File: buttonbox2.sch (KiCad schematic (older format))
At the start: 58 parts, among them J2 AVR-PDI-6, J4 Conn_01x03_Male, SW1 SW_SP3T, SW10 SW_Push, SW11 SW_Push, SW12 SW_Push, SW13 SW_Push, SW14 SW_Push, SW15 SW_Push, SW16 SW_Push, SW17 SW_Push, SW18 SW_Push, SW19 SW_Push, SW20 SW_Push, SW21 SW_Push, SW22 SW_Push, SW23 SW_Push, SW24 SW_Push, SW25 SW_Push, SW26 SW_Push, SW27 SW_Push, SW28 SW_Push, SW29 SW_Push, SW30 SW_Push, SW31 SW_Push, SW32 SW_Push, SW33 SW_Push, SW34 SW_Push, SW35 SW_Push, SW36 SW_Push, SW37 SW_Push, SW38 SW_Push, SW39 SW_Push, SW40 SW_Push, SW5 SW_Push, SW6 SW_Push, SW7 SW_Push, SW8 SW_Push, SW9 SW_Push, U1 ATxmega256A3-AU, U6 AMS1117-3.3, Y2 Crystal_GND24

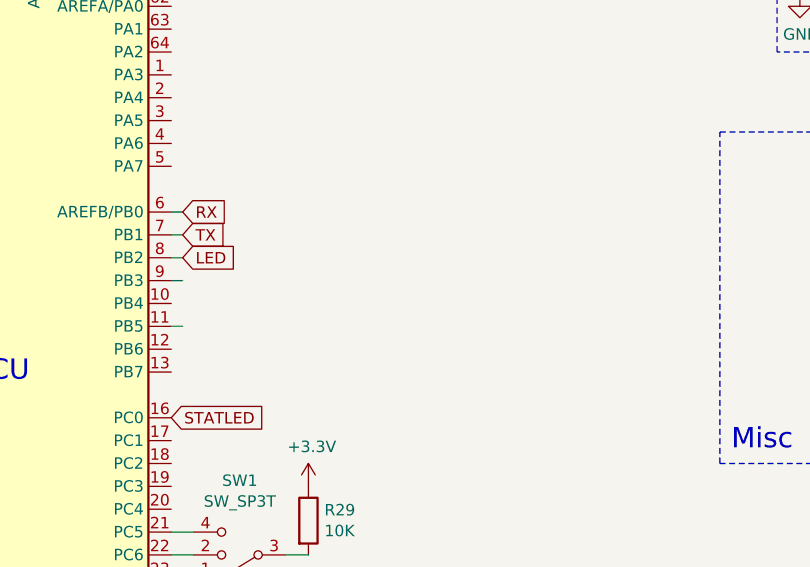
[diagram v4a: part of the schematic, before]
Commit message: Added a rotary encoder and almost all BC values
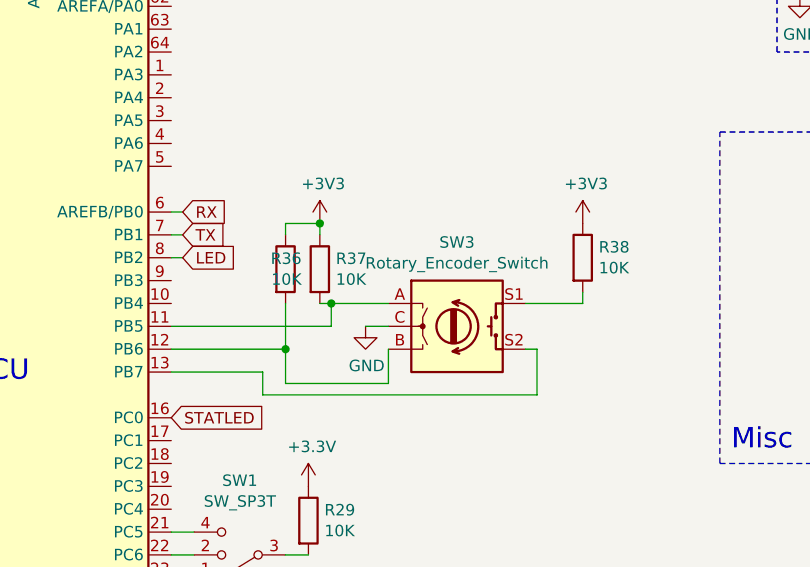
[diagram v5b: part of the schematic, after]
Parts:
- added R36, R37, R38: 10K, Resistor_SMD:R_0805_2012Metric, symbol Device:R
- added SW3: Rotary_Encoder_Switch, Rotary_Encoder:RotaryEncoder_Alps_EC11E-Switch_Vertical_H20mm_CircularMountingHoles, symbol Device:Rotary_Encoder_Switch
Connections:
- net +3V3: now also R36.1, R37.1, R38.1
- net GND: now also SW3.C
- net at U1.11 (PB5): now also R37.2, SW3.A
- net at U1.12 (PB6): now also R36.2, SW3.B
- net at U1.13 (PB7): now also SW3.S2
- new net: R38.2, SW3.S1
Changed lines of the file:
@@
 	2600 1200 2600 1100
 Connection ~ 2600 1200
-Wire Wire Line
-	3350 2750 3300 2750
-Wire Wire Line
-	3300 2950 3350 2950
 $Comp
 L power:GND #PWR04
@@
 	1350 2100 1900 2100
 Connection ~ 750  2100
+$Comp
+L Device:Rotary_Encoder_Switch SW3
+U 1 1 60C1C70F
+P 4550 2950
+F 0 "SW3" H 4550 3317 50  0000 C CNN
+F 1 "Rotary_Encoder_Switch" H 4550 3226 50  0000 C CNN
+F 2 "Rotary_Encoder:RotaryEncoder_Alps_EC11E-Switch_Vertical_H20mm_CircularMountingHoles" H 4400 3110 50  0001 C CNN
+F 3 "~" H 4550 3210 50  0001 C CNN
+	1    4550 2950
+	1    0    0    -1
+$EndComp
+$Comp
+L power:+3V3 #PWR054
+U 1 1 60CA26ED
+P 3950 2500
+F 0 "#PWR054" H 3950 2350 50  0001 C CNN
+F 1 "+3V3" H 3965 2673 50  0000 C CNN
+F 2 "" H 3950 2500 50  0001 C CNN
+F 3 "" H 3950 2500 50  0001 C CNN
+	1    3950 2500
+	1    0    0    -1
+$EndComp
+$Comp
+L power:GND #PWR055
+U 1 1 60CA3341
+P 4150 2950
+F 0 "#PWR055" H 4150 2700 50  0001 C CNN
+F 1 "GND" H 4155 2777 50  0000 C CNN
+F 2 "" H 4150 2950 50  0001 C CNN
+F 3 "" H 4150 2950 50  0001 C CNN
+	1    4150 2950
+	1    0    0    -1
+$EndComp
+Wire Wire Line
+	4250 2950 4150 2950
+$Comp
+L Device:R R37
+U 1 1 60CC5806
+P 3950 2700
+F 0 "R37" H 4020 2746 50  0000 L CNN
+F 1 "10K" H 4020 2655 50  0000 L CNN
+F 2 "Resistor_SMD:R_0805_2012Metric" V 3880 2700 50  0001 C CNN
+F 3 "~" H 3950 2700 50  0001 C CNN
+	1    3950 2700
+	1    0    0    -1
+$EndComp
+Wire Wire Line
+	3950 2850 4000 2850
+$Comp
+L Device:R R36
+U 1 1 60CFB51D
+P 3800 2700
+F 0 "R36" H 3870 2746 50  0000 R CNN
+F 1 "10K" H 3870 2655 50  0000 R CNN
+F 2 "Resistor_SMD:R_0805_2012Metric" V 3730 2700 50  0001 C CNN
+F 3 "~" H 3800 2700 50  0001 C CNN
+	1    3800 2700
+	1    0    0    -1
+$EndComp
+Wire Wire Line
+	3800 2550 3800 2500
+Wire Wire Line
+	3800 2500 3950 2500
+Wire Wire Line
+	3950 2550 3950 2500
+Connection ~ 3950 2500
+Wire Wire Line
+	4250 3050 4250 3200
+Wire Wire Line
+	4250 3200 3800 3200
+Wire Wire Line
+	3800 3200 3800 3050
+Wire Wire Line
+	4000 2850 4000 2950
+Wire Wire Line
+	4000 2950 3300 2950
+Connection ~ 4000 2850
+Wire Wire Line
+	4000 2850 4250 2850
+Wire Wire Line
+	3800 3050 3300 3050
+Connection ~ 3800 3050
+Wire Wire Line
+	3800 3050 3800 2850
+$Comp
+L power:+3V3 #PWR056
+U 1 1 60D421AA
+P 5100 2500
+F 0 "#PWR056" H 5100 2350 50  0001 C CNN
+F 1 "+3V3" H 5115 2673 50  0000 C CNN
+F 2 "" H 5100 2500 50  0001 C CNN
+F 3 "" H 5100 2500 50  0001 C CNN
+	1    5100 2500
+	1    0    0    -1
+$EndComp
+Wire Wire Line
+	4850 2850 5100 2850
+Wire Wire Line
+	5100 2850 5100 2800
+Wire Wire Line
+	4900 3050 4900 3250
+Wire Wire Line
+	3700 3250 3700 3150
+Wire Wire Line
+	3700 3150 3300 3150
+Wire Wire Line
+	4850 3050 4900 3050
+Wire Wire Line
+	3700 3250 4900 3250
+$Comp
+L Device:R R38
+U 1 1 60D8FC06
+P 5100 2650
+F 0 "R38" H 5170 2696 50  0000 L CNN
+F 1 "10K" H 5170 2605 50  0000 L CNN
+F 2 "Resistor_SMD:R_0805_2012Metric" V 5030 2650 50  0001 C CNN
+F 3 "~" H 5100 2650 50  0001 C CNN
+	1    5100 2650
+	1    0    0    -1
+$EndComp
 $EndSCHEMATC

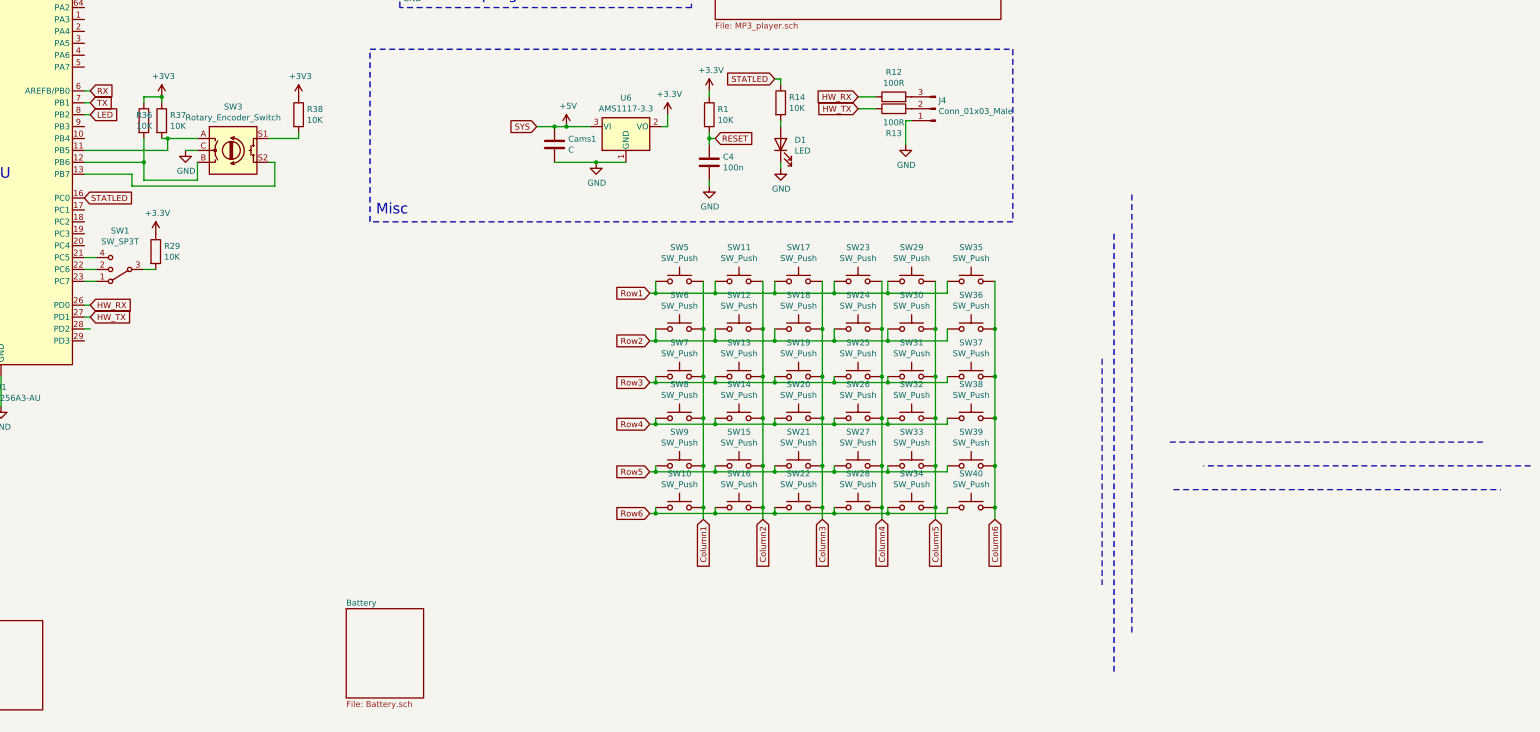
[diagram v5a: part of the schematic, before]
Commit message: Final schematic edits, PCB layout
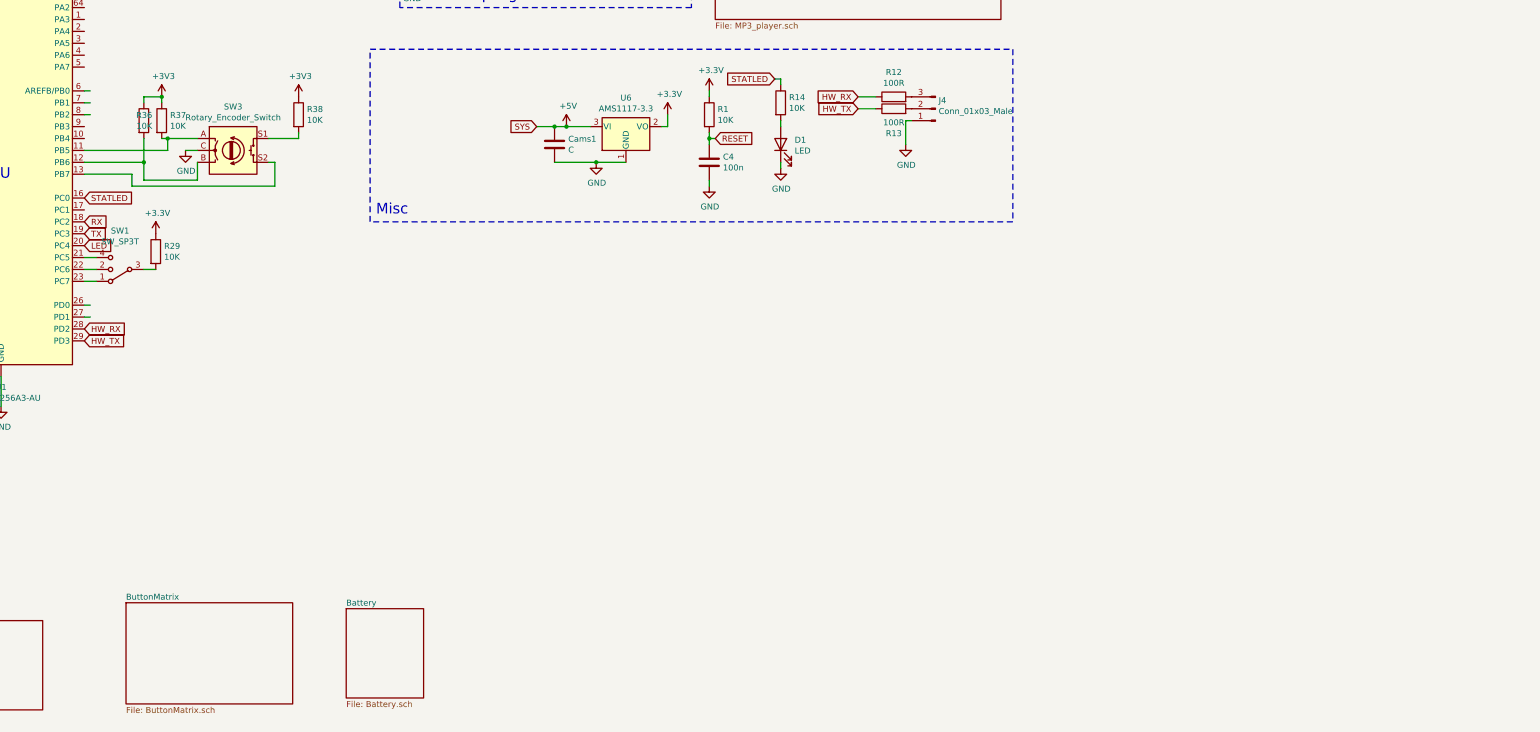
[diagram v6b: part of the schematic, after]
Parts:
- removed SW10, SW11, SW12, SW13, SW14, SW15, SW16, SW17, SW18, SW19, SW20, SW21, SW22, SW23, SW24, SW25, SW26, SW27, SW28, SW29, SW30, SW31, SW32, SW33, SW34, SW35, SW36, SW37, SW38, SW39, SW40, SW5, SW6, SW7, SW8, SW9: SW_Push, Hardware:SW_Cherry_MX_1.00u_PCB_BETTER, symbol Switch:SW_Push
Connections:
- wire segments 209 -> 100

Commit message: pretty much routed everything
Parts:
- added C37, C38, C39: 100n, Capacitor_SMD:C_0805_2012Metric, symbol Device:C
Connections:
- wire segments 100 -> 106
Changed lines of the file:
@@
 	4250 3050 4250 3200
 Wire Wire Line
-	4250 3200 3800 3200
+	4250 3200 4100 3200
 Wire Wire Line
 	3800 3200 3800 3050
@@
 Connection ~ 4000 2850
 Wire Wire Line
-	4000 2850 4250 2850
-Wire Wire Line
-	3800 3050 3300 3050
+	4000 2850 4150 2850
 Connection ~ 3800 3050
 Wire Wire Line
@@
 Wire Wire Line
 	4850 3050 4900 3050
-Wire Wire Line
-	3700 3250 4900 3250
 $Comp
 L Device:R R38
@@
 F1 "ButtonMatrix.sch" 50
 $EndSheet
+$Comp
+L Device:C C38
+U 1 1 610B68E6
+P 4150 2700
+F 0 "C38" H 4265 2746 50  0000 L CNN
+F 1 "100n" H 4265 2655 50  0000 L CNN
+F 2 "Capacitor_SMD:C_0805_2012Metric" H 4188 2550 50  0001 C CNN
+F 3 "~" H 4150 2700 50  0001 C CNN
+	1    4150 2700
+	1    0    0    -1
+$EndComp
+Connection ~ 4150 2850
+Wire Wire Line
+	4150 2850 4250 2850
+$Comp
+L Device:C C37
+U 1 1 610B785E
+P 4100 3350
+F 0 "C37" H 4215 3396 50  0000 L CNN
+F 1 "100n" H 4215 3305 50  0000 L CNN
+F 2 "Capacitor_SMD:C_0805_2012Metric" H 4138 3200 50  0001 C CNN
+F 3 "~" H 4100 3350 50  0001 C CNN
+	1    4100 3350
+	1    0    0    -1
+$EndComp
+Connection ~ 4100 3200
+Wire Wire Line
+	4100 3200 3800 3200
+Wire Wire Line
+	3300 3050 3800 3050
+$Comp
+L power:GND #PWR057
+U 1 1 610BB4E5
+P 4100 3500
+F 0 "#PWR057" H 4100 3250 50  0001 C CNN
+F 1 "GND" H 4105 3327 50  0000 C CNN
+F 2 "" H 4100 3500 50  0001 C CNN
+F 3 "" H 4100 3500 50  0001 C CNN
+	1    4100 3500
+	1    0    0    -1
+$EndComp
+$Comp
+L power:GND #PWR058
+U 1 1 610BBB62
+P 4400 2400
+F 0 "#PWR058" H 4400 2150 50  0001 C CNN
+F 1 "GND" H 4405 2227 50  0000 C CNN
+F 2 "" H 4400 2400 50  0001 C CNN
+F 3 "" H 4400 2400 50  0001 C CNN
+	1    4400 2400
+	1    0    0    -1
+$EndComp
+$Comp
+L power:GND #PWR059
+U 1 1 610BC44A
+P 4850 3550
+F 0 "#PWR059" H 4850 3300 50  0001 C CNN
+F 1 "GND" H 4855 3377 50  0000 C CNN
+F 2 "" H 4850 3550 50  0001 C CNN
+F 3 "" H 4850 3550 50  0001 C CNN
+	1    4850 3550
+	1    0    0    -1
+$EndComp
+Wire Wire Line
+	4150 2300 4150 2550
+Wire Wire Line
+	4150 2300 4400 2300
+Wire Wire Line
+	4400 2300 4400 2400
+Wire Wire Line
+	3700 3250 4850 3250
+$Comp
+L Device:C C39
+U 1 1 610D8766
+P 4850 3400
+F 0 "C39" H 4965 3446 50  0000 L CNN
+F 1 "100n" H 4965 3355 50  0000 L CNN
+F 2 "Capacitor_SMD:C_0805_2012Metric" H 4888 3250 50  0001 C CNN
+F 3 "~" H 4850 3400 50  0001 C CNN
+	1    4850 3400
+	1    0    0    -1
+$EndComp
+Connection ~ 4850 3250
+Wire Wire Line
+	4850 3250 4900 3250
 $EndSCHEMATC

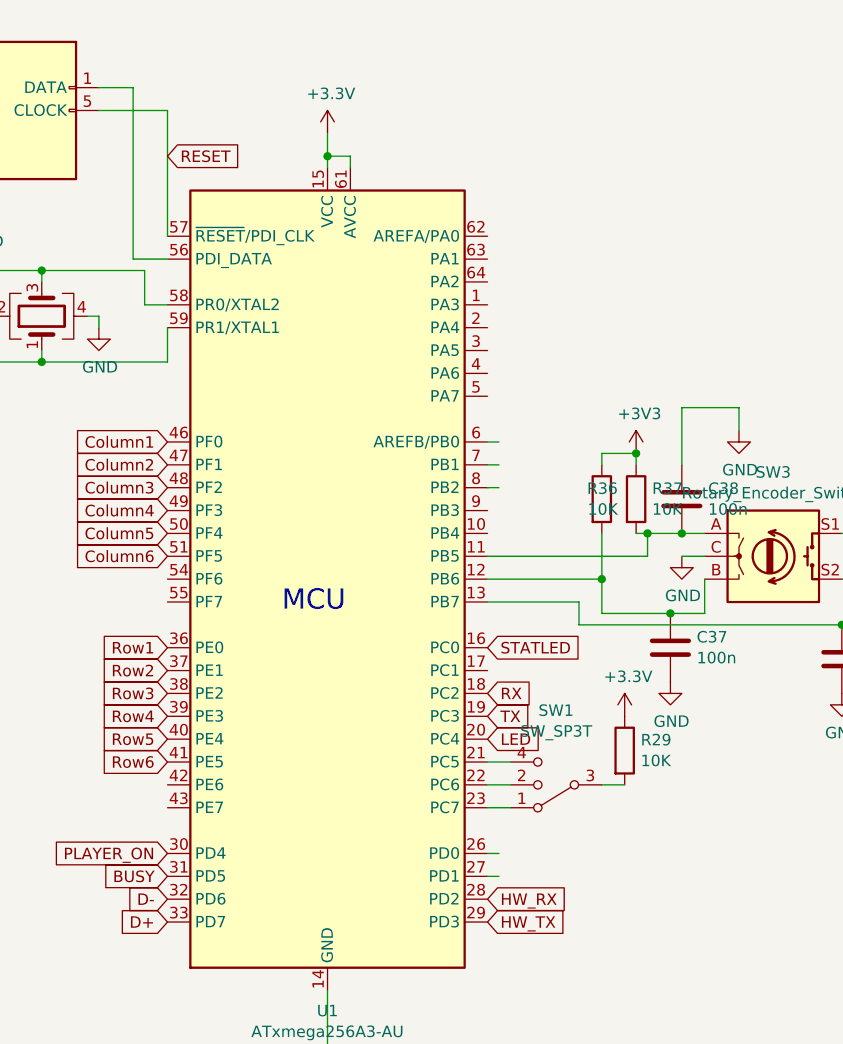
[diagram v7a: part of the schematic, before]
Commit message: Fixed some DRC errors and some incorrect wiring
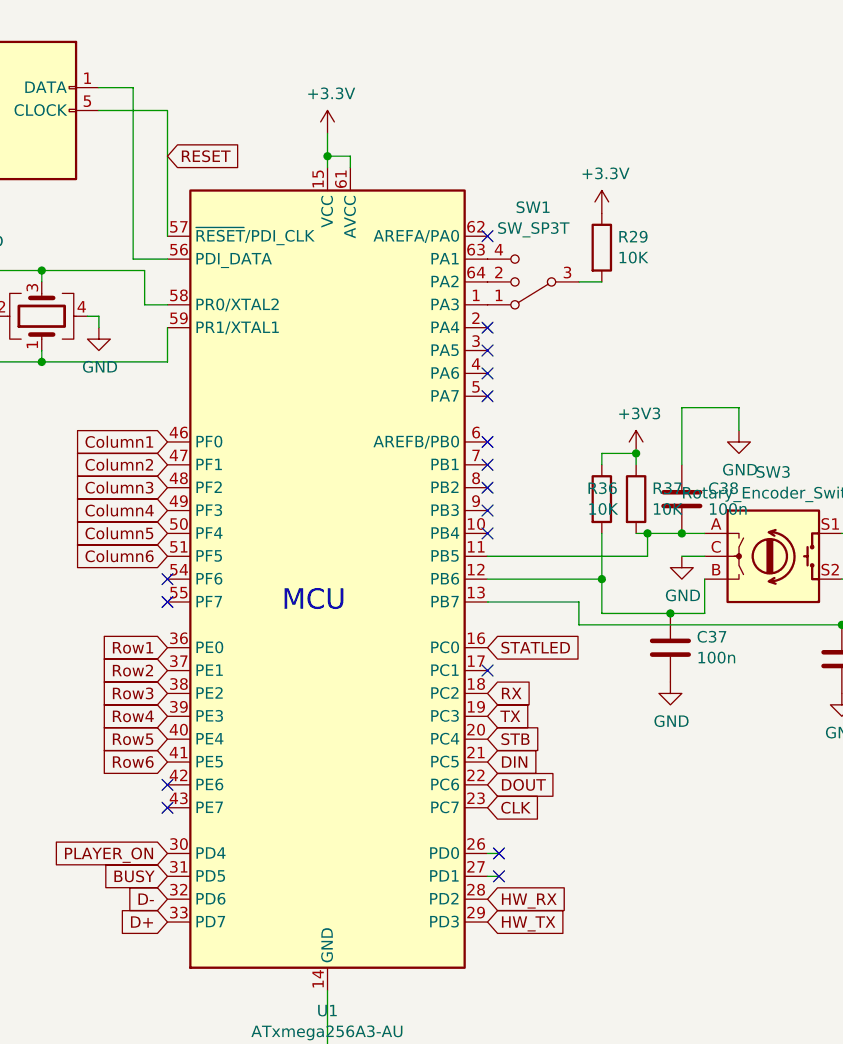
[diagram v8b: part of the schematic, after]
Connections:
- net labels added: CLK, DIN, DOUT, STB
- net labels removed: LED
- wire segments 106 -> 100
- no-connect marks 0 -> 17
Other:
- moved on the sheet: R29, SW1
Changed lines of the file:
@@
 Wire Wire Line
 	6850 1400 6850 1450
-Text GLabel 3300 3750 2    50   Input ~ 0
-LED
 Text GLabel 3300 3650 2    50   Input ~ 0
 TX
-Wire Wire Line
-	3350 2550 3300 2550
-Wire Wire Line
-	3350 2450 3300 2450
 Text GLabel 3300 3550 2    50   Input ~ 0
 RX
-Wire Wire Line
-	3300 2650 3350 2650
 Text GLabel 1900 4350 0    50   Input ~ 0
 BUSY
@@
 Text Notes 2400 3200 0    89   ~ 0
 MCU
-Wire Wire Line
-	2600 5100 2600 4850
-Wire Wire Line
-	1900 1950 1900 2100
 $Comp
 L power:GND #PWR019
@@
 	1    0    0    -1
 $EndComp
-$Comp
-L MCU_Microchip_ATmega:ATxmega256A3-AU U1
-U 1 1 619EAF40
-P 2600 3050
-F 0 "U1" H 2600 1161 50  0000 C CNN
-F 1 "ATxmega256A3-AU" H 2600 1070 50  0000 C CNN
-F 2 "Package_QFP:TQFP-64_14x14mm_P0.8mm" H 2600 3050 50  0001 C CIN
-F 3 "http://ww1.microchip.com/downloads/en/DeviceDoc/Atmel-8068-8-and16-bit-AVR-XMEGA-A3-Microcontrollers_Datasheet.pdf" H 2600 3050 50  0001 C CNN
-	1    2600 3050
-	1    0    0    -1
-$EndComp
 $Sheet
 S 5500 6800 650  750
@@
 L Switch:SW_SP3T SW1
 U 1 1 60FDF2D6
-P 3600 3950
-F 0 "SW1" H 3600 3625 50  0000 C CNN
-F 1 "SW_SP3T" H 3600 3716 50  0000 C CNN
-F 2 "Hardware:schakelaar" H 2975 4125 50  0001 C CNN
-F 3 "~" H 2975 4125 50  0001 C CNN
-	1    3600 3950
+P 3500 1750
+F 0 "SW1" H 3500 1425 50  0000 C CNN
+F 1 "SW_SP3T" H 3500 1516 50  0000 C CNN
+F 2 "Hardware:schakelaar" H 2875 1925 50  0001 C CNN
+F 3 "~" H 2875 1925 50  0001 C CNN
+	1    3500 1750
 	-1   0    0    1
 $EndComp
-Wire Wire Line
-	3300 4050 3400 4050
-Wire Wire Line
-	3300 3950 3400 3950
-Wire Wire Line
-	3300 3850 3400 3850
 $Comp
 L Device:R R29
 U 1 1 61000DFD
-P 3900 3800
-F 0 "R29" H 3970 3846 50  0000 L CNN
-F 1 "10K" H 3970 3755 50  0000 L CNN
-F 2 "Resistor_SMD:R_0805_2012Metric" V 3830 3800 50  0001 C CNN
-F 3 "~" H 3900 3800 50  0001 C CNN
-	1    3900 3800
-	1    0    0    -1
-$EndComp
-Wire Wire Line
-	3800 3950 3900 3950
+P 3800 1600
+F 0 "R29" H 3870 1646 50  0000 L CNN
+F 1 "10K" H 3870 1555 50  0000 L CNN
+F 2 "Resistor_SMD:R_0805_2012Metric" V 3730 1600 50  0001 C CNN
+F 3 "~" H 3800 1600 50  0001 C CNN
+	1    3800 1600
+	1    0    0    -1
+$EndComp
+Wire Wire Line
+	3700 1750 3800 1750
 $Comp
 L power:+3.3V #PWR051
 U 1 1 6100C306
-P 3900 3650
-F 0 "#PWR051" H 3900 3500 50  0001 C CNN
-F 1 "+3.3V" H 3915 3823 50  0000 C CNN
-F 2 "" H 3900 3650 50  0001 C CNN
-F 3 "" H 3900 3650 50  0001 C CNN
-	1    3900 3650
+P 3800 1450
+F 0 "#PWR051" H 3800 1300 50  0001 C CNN
+F 1 "+3.3V" H 3815 1623 50  0000 C CNN
+F 2 "" H 3800 1450 50  0001 C CNN
+F 3 "" H 3800 1450 50  0001 C CNN
+	1    3800 1450
 	1    0    0    -1
 $EndComp
@@
 Wire Wire Line
 	4850 3250 4900 3250
+NoConn ~ 3350 4250
+NoConn ~ 3350 4350
+NoConn ~ 1900 3950
+NoConn ~ 1900 4050
+NoConn ~ 1900 3050
+NoConn ~ 1900 3150
+Wire Wire Line
+	2600 5100 2600 4850
+Wire Wire Line
+	1900 1950 1900 2100
+$Comp
+L MCU_Microchip_ATmega:ATxmega256A3-AU U1
+U 1 1 619EAF40
+P 2600 3050
+F 0 "U1" H 2600 1161 50  0000 C CNN
+F 1 "ATxmega256A3-AU" H 2600 1070 50  0000 C CNN
+F 2 "Package_QFP:TQFP-64_14x14mm_P0.8mm" H 2600 3050 50  0001 C CIN
+F 3 "http://ww1.microchip.com/downloads/en/DeviceDoc/Atmel-8068-8-and16-bit-AVR-XMEGA-A3-Microcontrollers_Datasheet.pdf" H 2600 3050 50  0001 C CNN
+	1    2600 3050
+	1    0    0    -1
+$EndComp
+NoConn ~ 3300 2450
+NoConn ~ 3300 2550
+NoConn ~ 3300 2650
+NoConn ~ 3300 2750
+NoConn ~ 3300 2850
+NoConn ~ 3300 2250
+NoConn ~ 3300 2150
+NoConn ~ 3300 2050
+NoConn ~ 3300 1950
+NoConn ~ 3300 1550
+Text GLabel 3300 3850 2    50   Input ~ 0
+DIN
+Text GLabel 3300 3950 2    50   Input ~ 0
+DOUT
+Text GLabel 3300 4050 2    50   Input ~ 0
+CLK
+Text GLabel 3300 3750 2    50   Input ~ 0
+STB
+NoConn ~ 3300 3450
 $EndSCHEMATC
